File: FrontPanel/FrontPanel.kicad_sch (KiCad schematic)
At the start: 76 parts, among them J1 CPU, J2 Backplane, J3 MPW-Y, J4 Conn_01x05_Female, SW1 SELECT, SW2 OPSYS, SW3 R/F, U1 74LS38, U2 74LS38, U3 74LS123, U4 NE555P

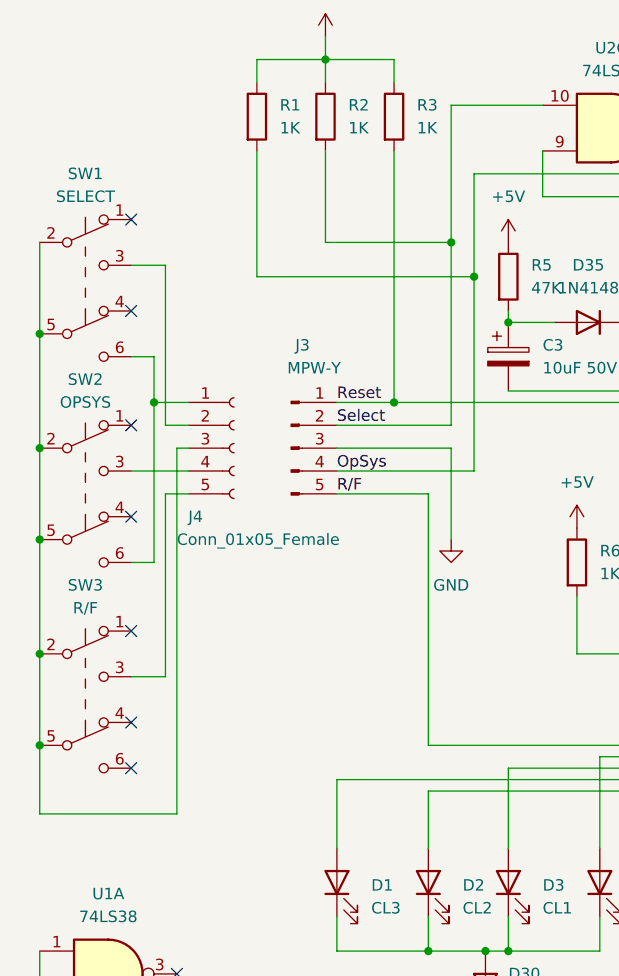
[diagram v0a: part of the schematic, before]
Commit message: FrontPanel: Buttons board
A preliminary design of a button board. Needs to be verified against actual
parts footprint.
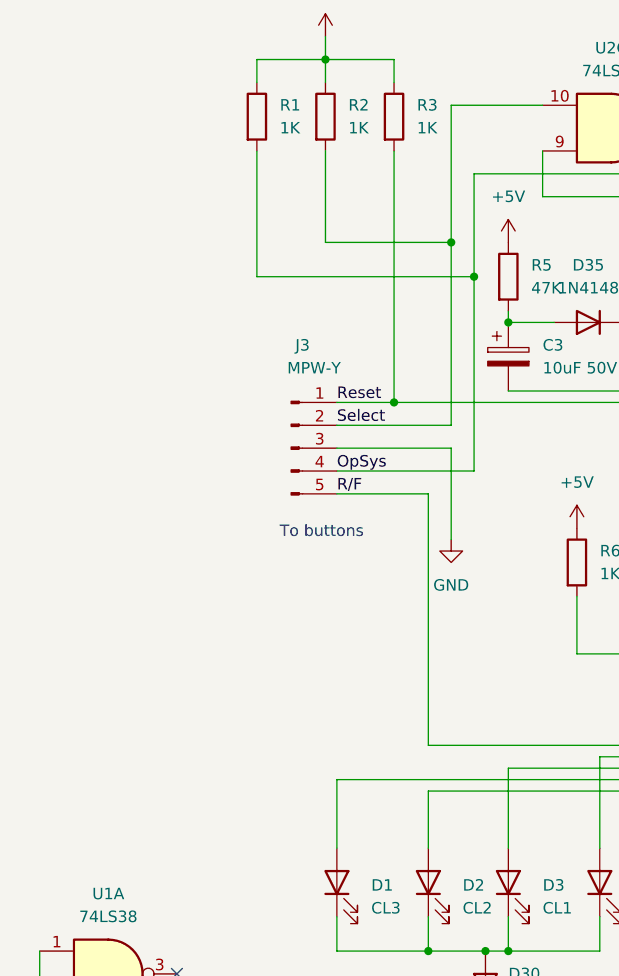
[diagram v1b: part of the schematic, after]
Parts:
- removed J4: Conn_01x05_Female, symbol Connector:Conn_01x05_Female
- removed SW1: SELECT, symbol Switch:SW_Push_DPDT
- removed SW2: OPSYS, symbol Switch:SW_Push_DPDT
- removed SW3: R/F, symbol Switch:SW_Push_DPDT
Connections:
- no-connect marks 18 -> 11
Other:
- note added: "To buttons"

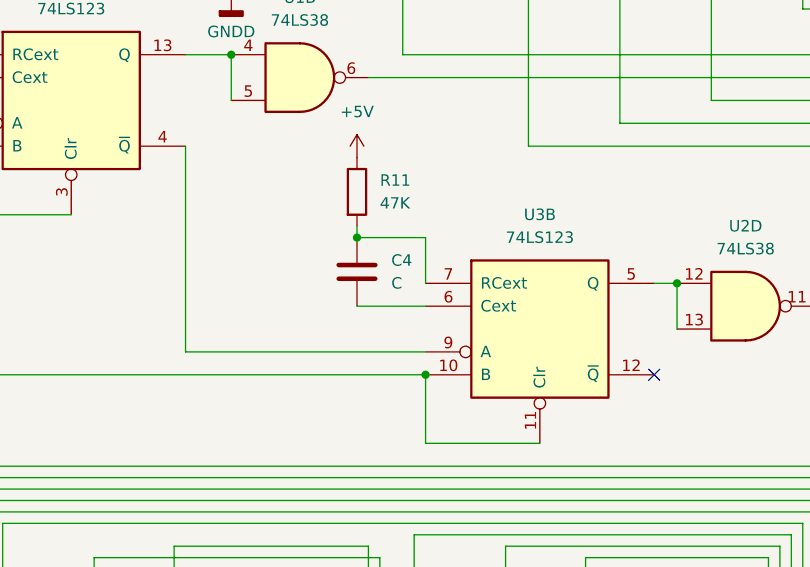
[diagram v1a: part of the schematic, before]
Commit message: FrontPanel: Provide C4 value
100 nanofarad, looked up by Nakazoto
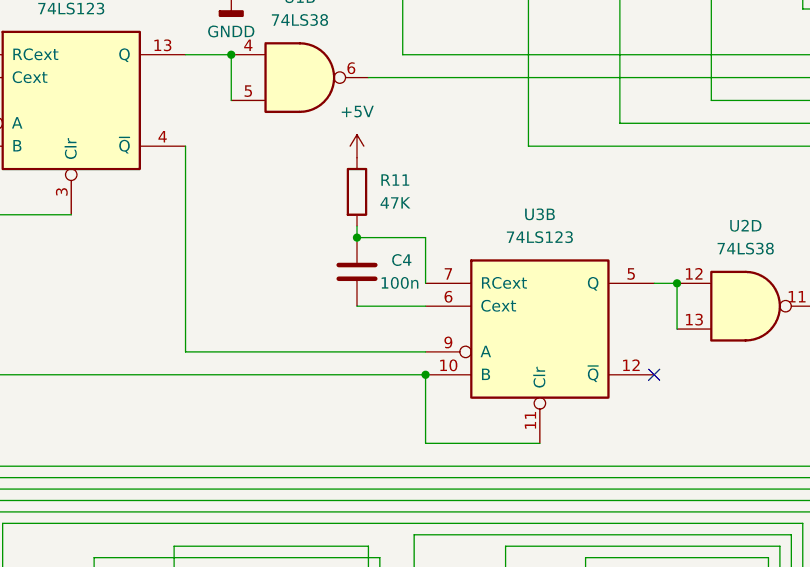
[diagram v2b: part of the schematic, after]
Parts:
- C4: value C -> 100n
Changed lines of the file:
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@@
   )
   (symbol (lib_id "Device:C") (at 129.54 77.47 0) (unit 1)
-    (in_bom yes) (on_board yes) (fields_autoplaced)
+    (in_bom yes) (on_board yes)
     (property "Reference" "C4" (id 0) (at 133.35 76.1999 0)
       (effects (font (size 1.27 1.27)) (justify left))
     )
-    (property "Value" "C" (id 1) (at 133.35 78.7399 0)
+    (property "Value" "100n" (id 1) (at 132.08 78.74 0)
       (effects (font (size 1.27 1.27)) (justify left))
     )
@@
     )
     (path "/faabe0a6-0893-4db9-9a88-dd51dd4ecae8"
-      (reference "C4") (unit 1) (value "C") (footprint "Capacitor_THT:C_Disc_D4.3mm_W1.9mm_P5.00mm")
+      (reference "C4") (unit 1) (value "100n") (footprint "Capacitor_THT:C_Disc_D4.3mm_W1.9mm_P5.00mm")
     )
     (path "/1d1adde6-10ec-445c-bd3e-c6903ed0b715"

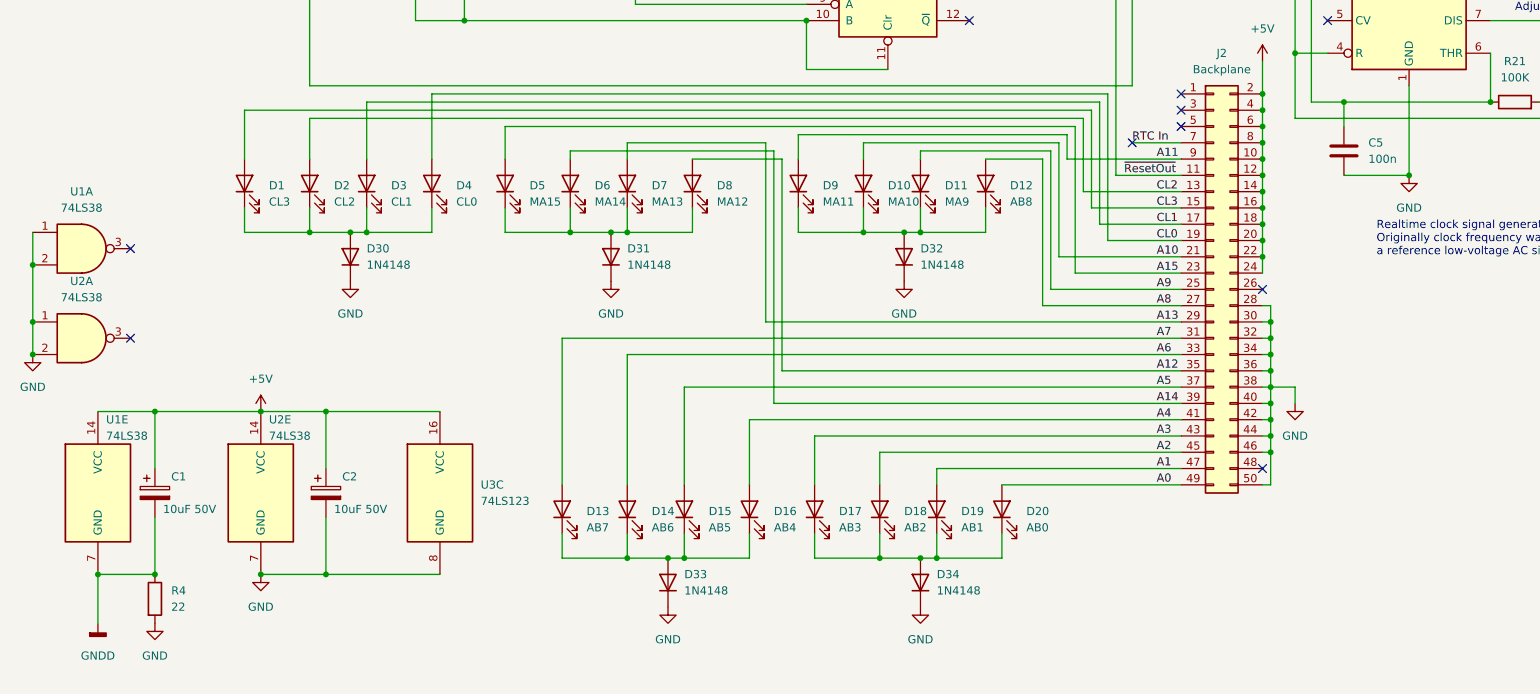
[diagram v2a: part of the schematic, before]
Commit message: FrontPanel: Improve ground separation
Follow the original idea and fully decouple GND from different connectors.
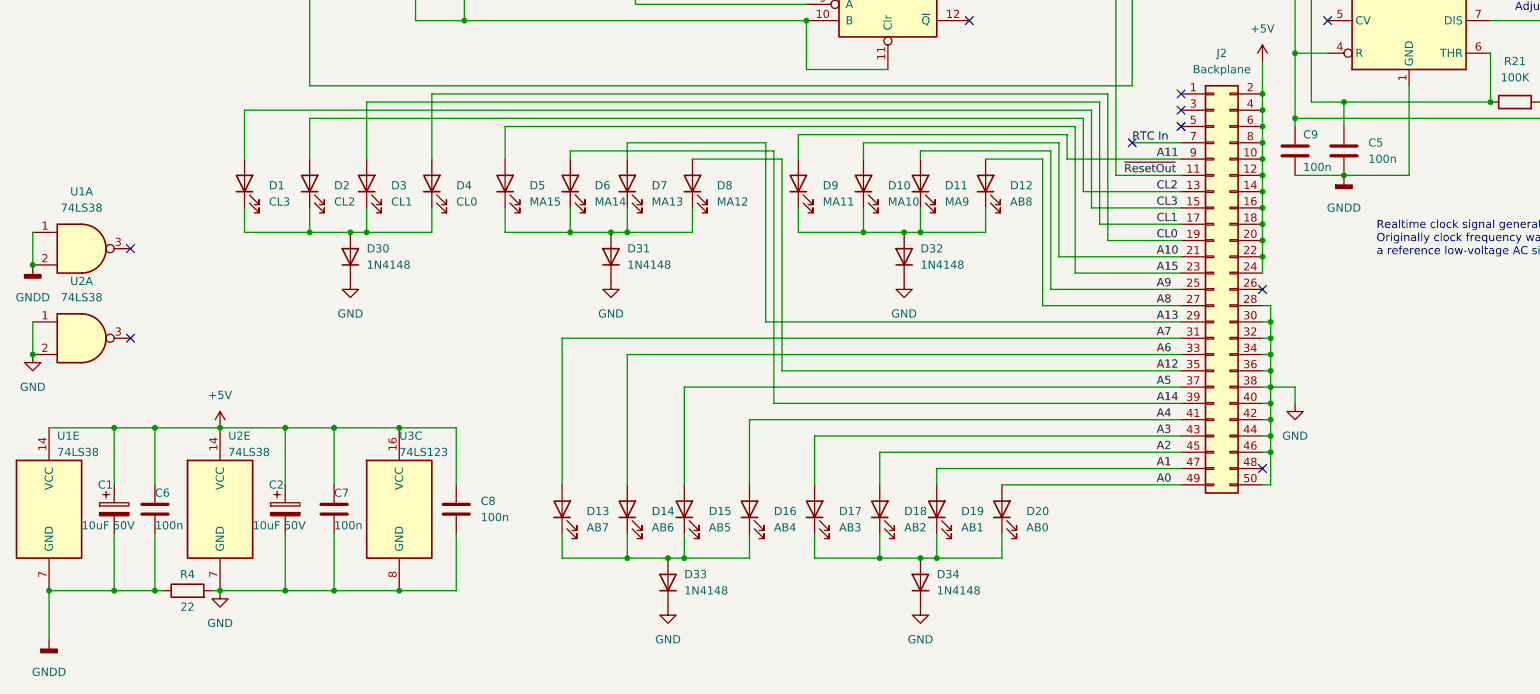
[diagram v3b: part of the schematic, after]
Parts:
- added C6, C7, C8, C9: 100n, Capacitor_THT:C_Disc_D4.3mm_W1.9mm_P5.00mm, symbol Device:C
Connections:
- net +5V: now also C6.1, C7.1, C8.1, C9.1
- net GND: now also C7.2, C8.2; no longer C5.2, U1.1, U1.2, U4.1 (GND)
- net GNDD: now also C5.2, U1.1, U1.2, U4.1 (GND), C6.2, C9.2
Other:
- title: (none) -> Centurion front panel replica
- moved on the sheet: C1, C2, R4, U1E, U2E, U3C

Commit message: FrontPanel: Erratum E001
Due to unverified assumptions in original schematic, power and ground separation
between connectors, which is actually present on original boards, wasn't done
correctly.
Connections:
- net +5V: no longer C1.1, C6.1, C9.1, D36.2 (A), J1.16 (Pin_16), J1.18 (Pin_18), J1.20 (Pin_20), J1.22 (Pin_22), J1.24 (Pin_24), J1.26 (Pin_26), R12.1, R13.1, R14.1, R15.1, R16.1, R17.1, R18.1, R19.1, R20.1, R22.2, R9.1, U1.14 (VCC), U4.4 (R), U4.8 (VCC)
- new net +5VD: C1.1, C6.1, C9.1, D36.2 (A), J1.16 (Pin_16), J1.18 (Pin_18), J1.20 (Pin_20), J1.22 (Pin_22), J1.24 (Pin_24), J1.26 (Pin_26), R12.1, R13.1, R14.1, R15.1, R16.1, R17.1, R18.1, R19.1, R20.1, R22.2, R9.1, U1.14 (VCC), U4.4 (R), U4.8 (VCC)
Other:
- moved on the sheet: J3, R23
